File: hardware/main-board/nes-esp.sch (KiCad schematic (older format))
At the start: 35 parts, among them J4 Program, J5 NHD OLED Connector, J6 microSD Socket, Q1 S8050, Q2 S8050, Q3 S8050, SW2 ESP Reset, U12 MCP7940N, U13 ESP-WROOM-32, U14 TSL251R, U15 EClamp2410P, Y2 32.768 kHz

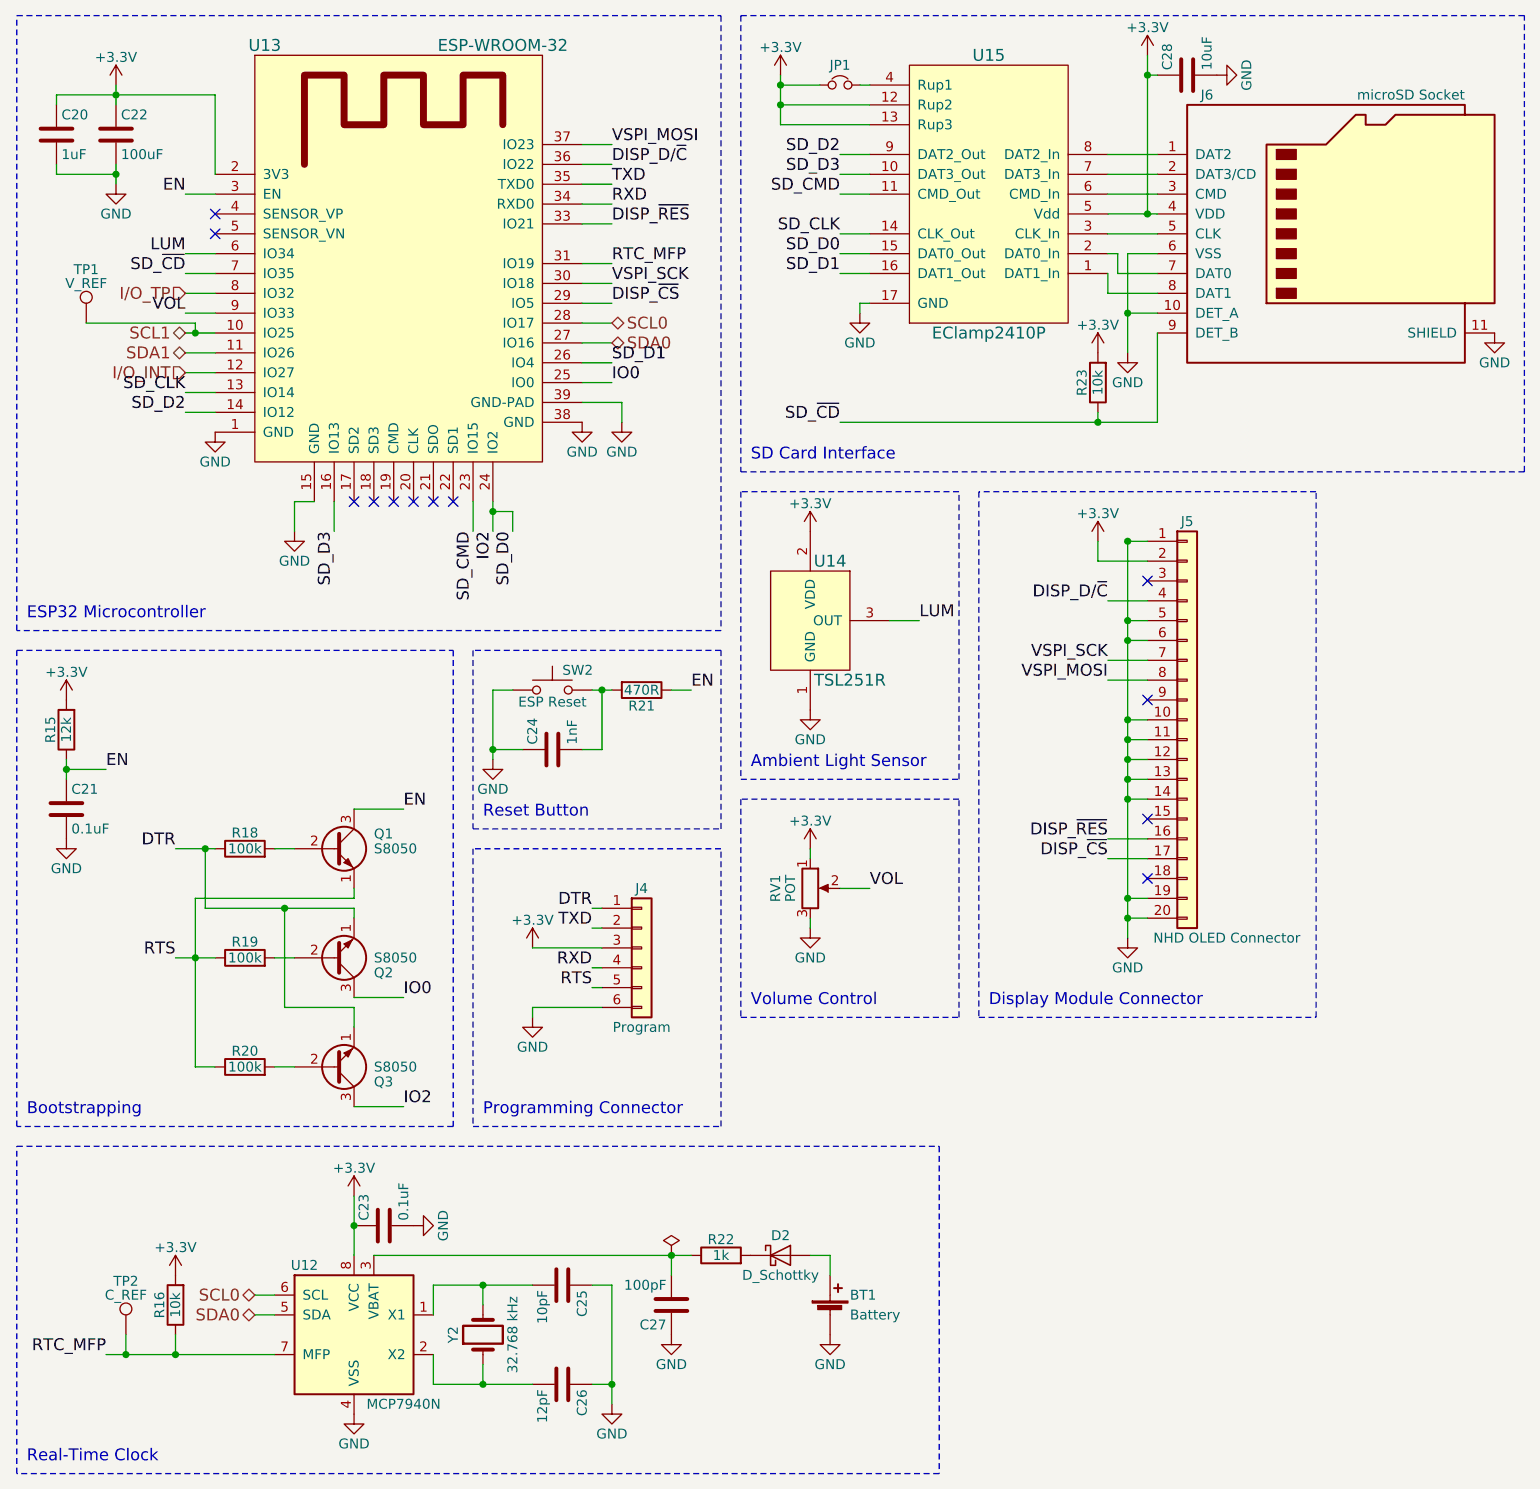
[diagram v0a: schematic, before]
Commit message: Remove the ambient light sensor from the main board
Fixes #9
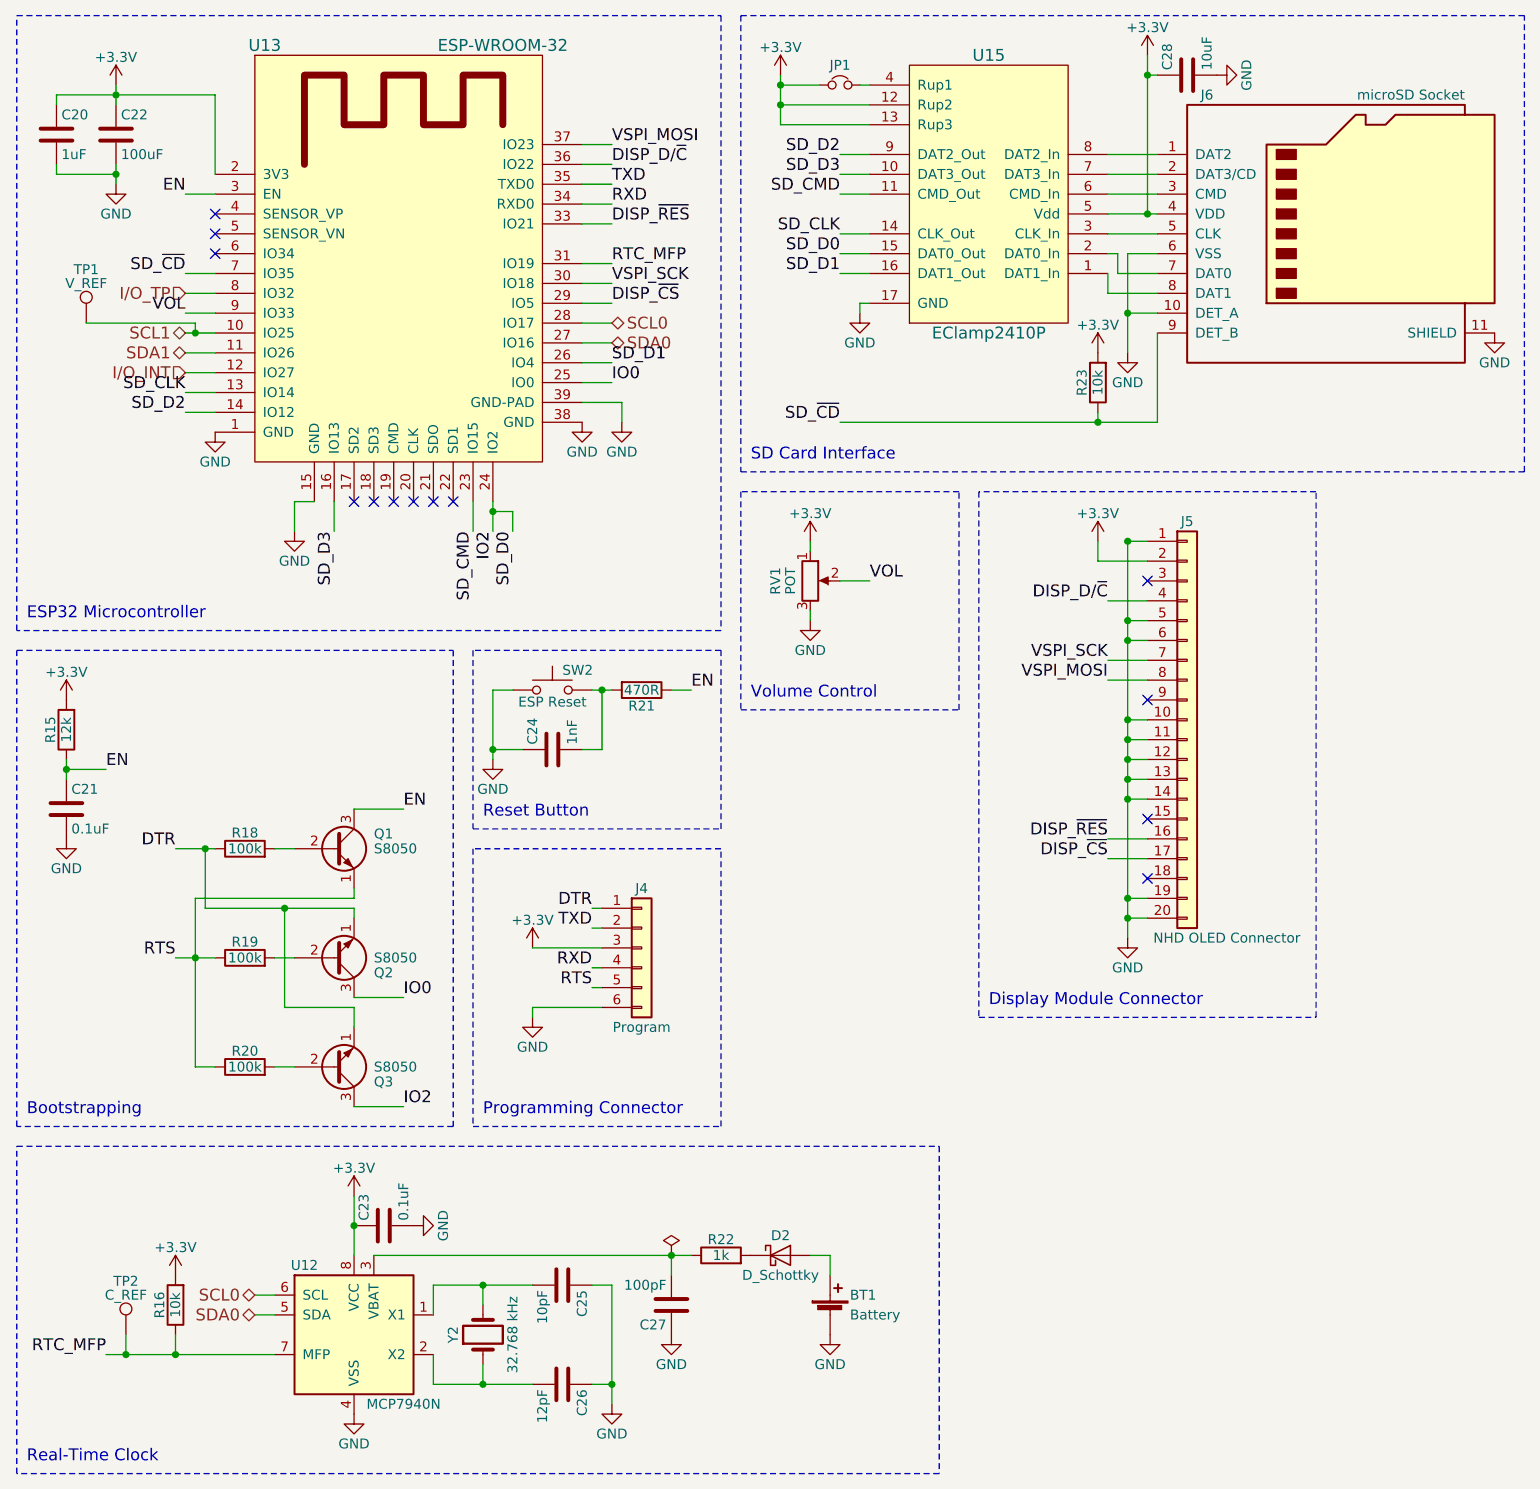
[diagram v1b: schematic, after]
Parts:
- removed U14: TSL251R, lib_fp:S-3, symbol TSL251R
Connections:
- net LUM: no longer names the net of U13.6 (IO34)
- no-connect marks 12 -> 13
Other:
- note removed: "Ambient Light Sensor"
- moved on the sheet: RV1

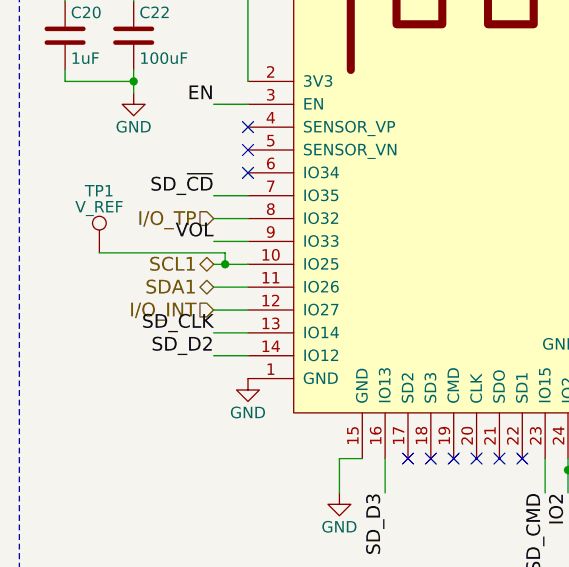
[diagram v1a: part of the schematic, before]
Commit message: Move TP1 over to GPIO27
This moves the ADC calibration test point from a pin that always has a
pull-up resistor, to one that only has issues if the input board is
plugged in.

Fixes #6
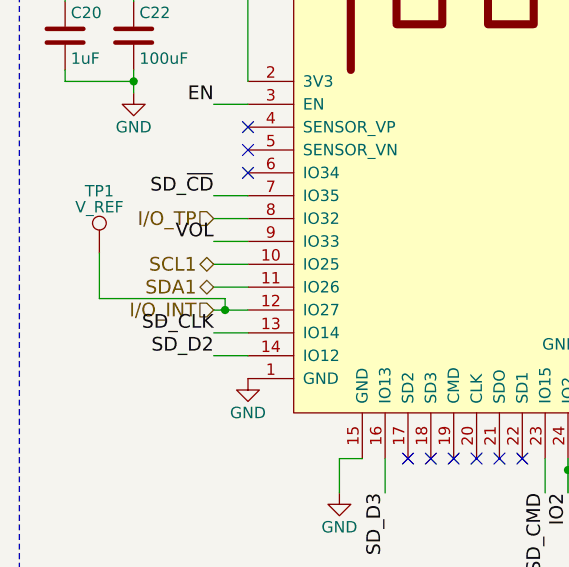
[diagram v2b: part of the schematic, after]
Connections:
- net I/O_INT: now also TP1.1
- net SCL1: no longer TP1.1
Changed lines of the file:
@@
 Wire Wire Line
 	1550 2250 1400 2250
-Wire Wire Line
-	1450 2150 1450 2100
-Wire Wire Line
-	1450 2100 900  2100
-Connection ~ 1450 2150
 Text HLabel 1400 2350 0    60   Input ~ 0
 I/O_INT
@@
 	7100 2950 5400 2950
 NoConn ~ 1550 1750
+Wire Wire Line
+	900  2100 900  2300
+Wire Wire Line
+	900  2300 1450 2300
+Wire Wire Line
+	1450 2300 1450 2350
+Connection ~ 1450 2350
 $EndSCHEMATC

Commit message: Create new component to fix Q1/Q2/Q3 pin mapping issues
Apparently the S8050 included in the KiCad library was for the TO-92
version of the part, for which the pin mapping was correct. The part
we're using is a SOT-23, more completely called SS8050, and has
different specifications. So fixing the issue meant creating a new
library symbol with the right pin assignments.

The PCB layout has also been updated to reflect this change.

Fixes #5
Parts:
- Q1, Q2, Q3: value S8050 -> SS8050; symbol S8050 -> SS8050
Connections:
- net DTR: now also Q2.2 (E), Q3.2 (E); no longer Q2.1 (E), Q3.1 (E)
- net RTS: now also Q1.2 (E); no longer Q1.1 (E)
- net at R18.2: now also Q1.1 (B); no longer Q1.2 (B)
- net at R19.2: now also Q2.1 (B); no longer Q2.2 (B)
- net at R20.2: now also Q3.1 (B); no longer Q3.2 (B)
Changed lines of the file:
@@
 $EndComp
 $Comp
-L S8050 Q1
+L SS8050 Q1
 U 1 1 5A7F7824
 P 2150 4750
 F 0 "Q1" H 2350 4825 50  0000 L CNN
-F 1 "S8050" H 2350 4750 50  0000 L CNN
+F 1 "SS8050" H 2350 4750 50  0000 L CNN
 F 2 "Package_TO_SOT_SMD:SOT-23" H 2350 4675 50  0001 L CIN
 F 3 "http://www.mccsemi.com/up_pdf/MMSS8050(SOT-23).pdf" H 2150 4750 50  0001 L CNN
@@
 $EndComp
 $Comp
-L S8050 Q2
+L SS8050 Q2
 U 1 1 5A7F7D3B
 P 2150 5300
 F 0 "Q2" H 2350 5375 50  0000 L CNN
-F 1 "S8050" H 2350 5300 50  0000 L CNN
+F 1 "SS8050" H 2350 5300 50  0000 L CNN
 F 2 "Package_TO_SOT_SMD:SOT-23" H 2350 5225 50  0001 L CIN
 F 3 "http://www.mccsemi.com/up_pdf/MMSS8050(SOT-23).pdf" H 2150 5300 50  0001 L CNN
@@
 $EndComp
 $Comp
-L S8050 Q3
+L SS8050 Q3
 U 1 1 5A7F7D98
 P 2150 5850
 F 0 "Q3" H 2350 5925 50  0000 L CNN
-F 1 "S8050" H 2350 5850 50  0000 L CNN
+F 1 "SS8050" H 2350 5850 50  0000 L CNN
 F 2 "Package_TO_SOT_SMD:SOT-23" H 2350 5775 50  0001 L CIN
 F 3 "http://www.mccsemi.com/up_pdf/MMSS8050(SOT-23).pdf" H 2150 5850 50  0001 L CNN

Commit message: Fixed 12k resistor component data
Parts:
- R15: Manufacturer PN CRCW080512K0FKEA -> CRCW080512K0JNEA; Supplier PN 541-12.0KCCT-ND -> 541-12KACT-ND
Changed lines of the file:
@@
 F 4 "RES SMD 12K OHM 1% 1/8W 0805" H 800 4150 60  0001 C CNN "Description"
 F 5 "Vishay Dale" H 800 4150 60  0001 C CNN "Manufacturer"
-F 6 "CRCW080512K0FKEA" H 800 4150 60  0001 C CNN "Manufacturer PN"
+F 6 "CRCW080512K0JNEA" H 800 4150 60  0001 C CNN "Manufacturer PN"
 F 7 "Digi-Key" H 880 4250 50  0001 C CNN "Supplier"
-F 8 "541-12.0KCCT-ND" H 800 4150 60  0001 C CNN "Supplier PN"
+F 8 "541-12KACT-ND" H 800 4150 60  0001 C CNN "Supplier PN"
 	1    800  4150
 	-1   0    0    1

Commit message: Update hardware project to support KiCad v5
This change does all the necessary symbol remapping and file re-saving
so that KiCad v5 is now cleanly supported going forward. Hopefully there
are no actual changes of consequence introduced by this diff.
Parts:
- BT1: symbol Battery_Cell -> Device:Battery_Cell
- C20, C21, C22, C23, C24, C25, C26, C27, C28: symbol C -> Device:C
- D2: symbol D_Schottky -> Device:D_Schottky
- J4: symbol Conn_01x06 -> Connector_Generic:Conn_01x06
- J5: symbol Conn_01x20 -> Connector_Generic:Conn_01x20
- J6: symbol Micro_SD_Card_Det_Hirose_DM3AT -> Connector:Micro_SD_Card_Det_Hirose_DM3AT
- JP1: symbol Jumper_NC_Small -> Device:Jumper_NC_Small
- Q1, Q2, Q3: symbol SS8050 -> nes:SS8050
- R15, R16, R18, R19, R20, R21, R22, R23: symbol R -> Device:R
- RV1: symbol POT -> Device:R_POT
- SW2: symbol SW_Push -> Switch:SW_Push
- TP1, TP2: symbol Test_Point -> Connector:TestPoint
- U12: symbol MCP7940N -> Timer:MCP7940N-xSN
- U13: symbol ESP32-WROOM -> ESP32-footprints-Shem-Lib:ESP32-WROOM
- U15: symbol EClamp2410P -> nes:EClamp2410P
- Y2: symbol Crystal -> Device:Crystal
